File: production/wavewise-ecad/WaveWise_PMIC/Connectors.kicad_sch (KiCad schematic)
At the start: 18 parts, among them J1 24V output, J11 Servo output, J12 Regulated 48V Input, J14 Battery Direct Input, J2 Inverter Inputs, J3 5031590300, J4 5031590400, J5 5031590400, J6 5031590400, J7 5V output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

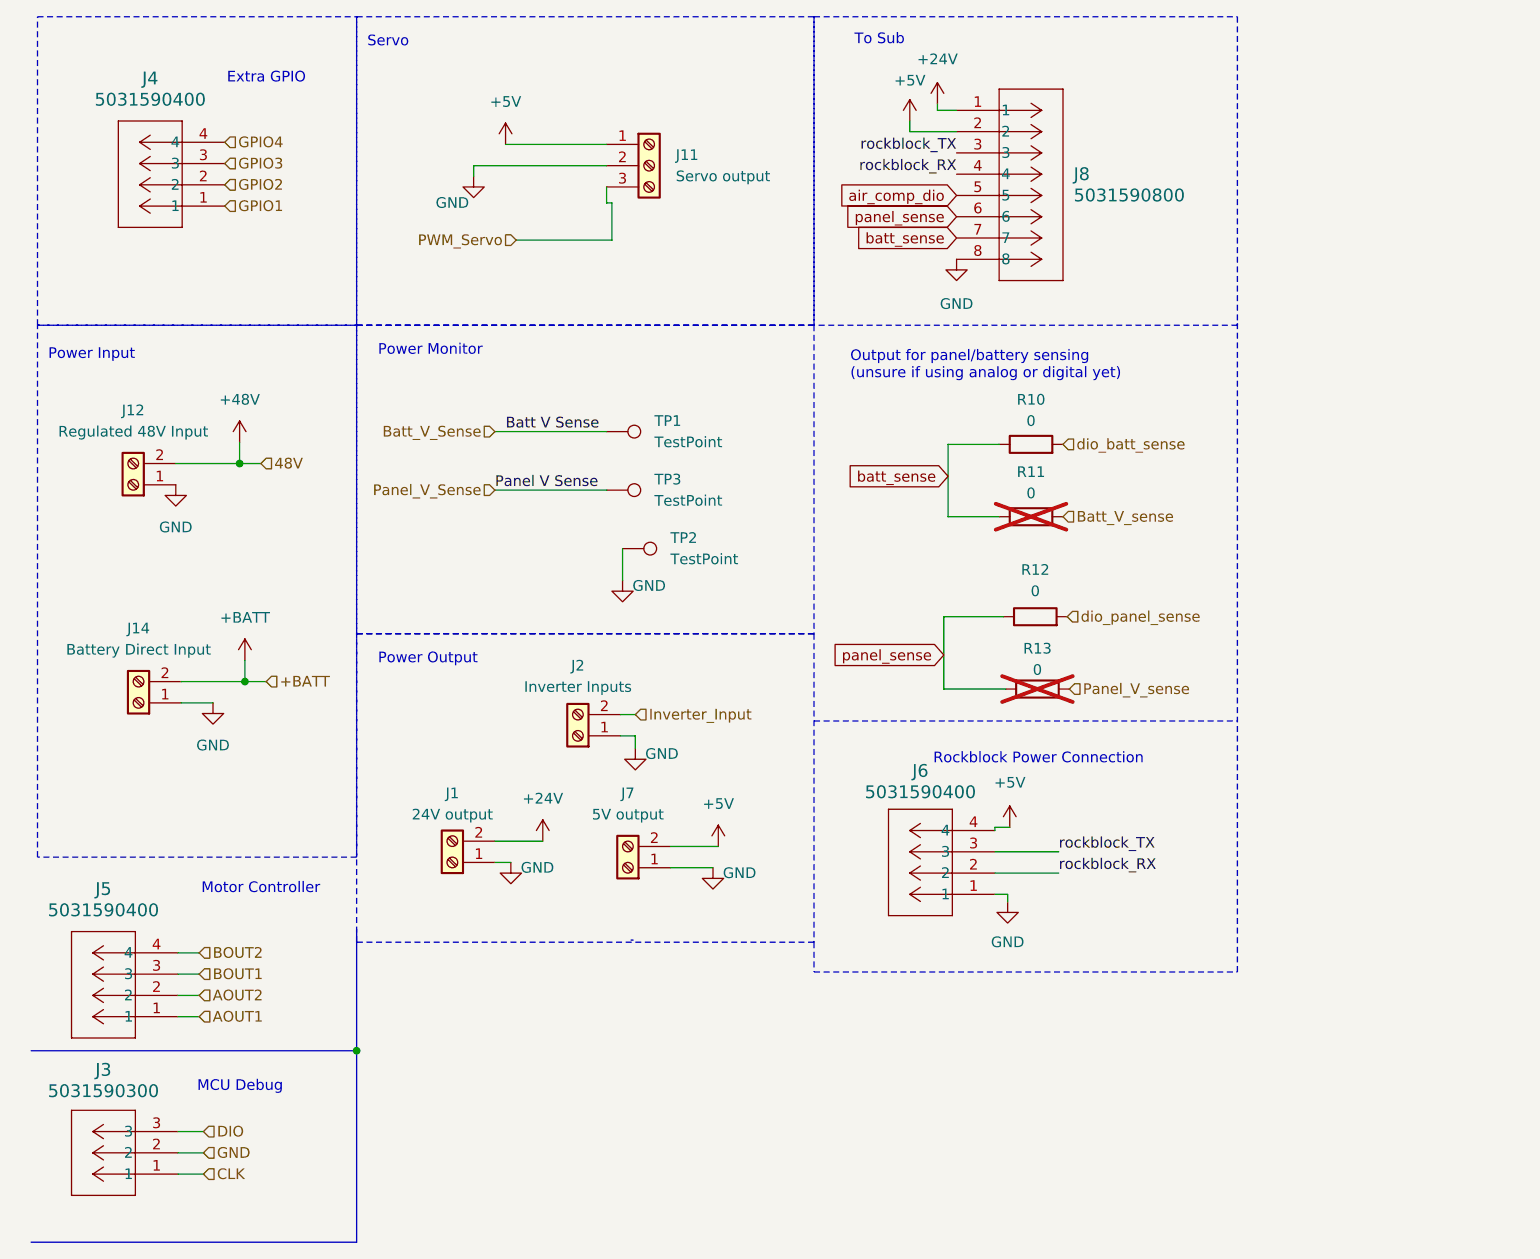
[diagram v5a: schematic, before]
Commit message: Rearranged the whole board
All done aside from no place resistor and  power planes
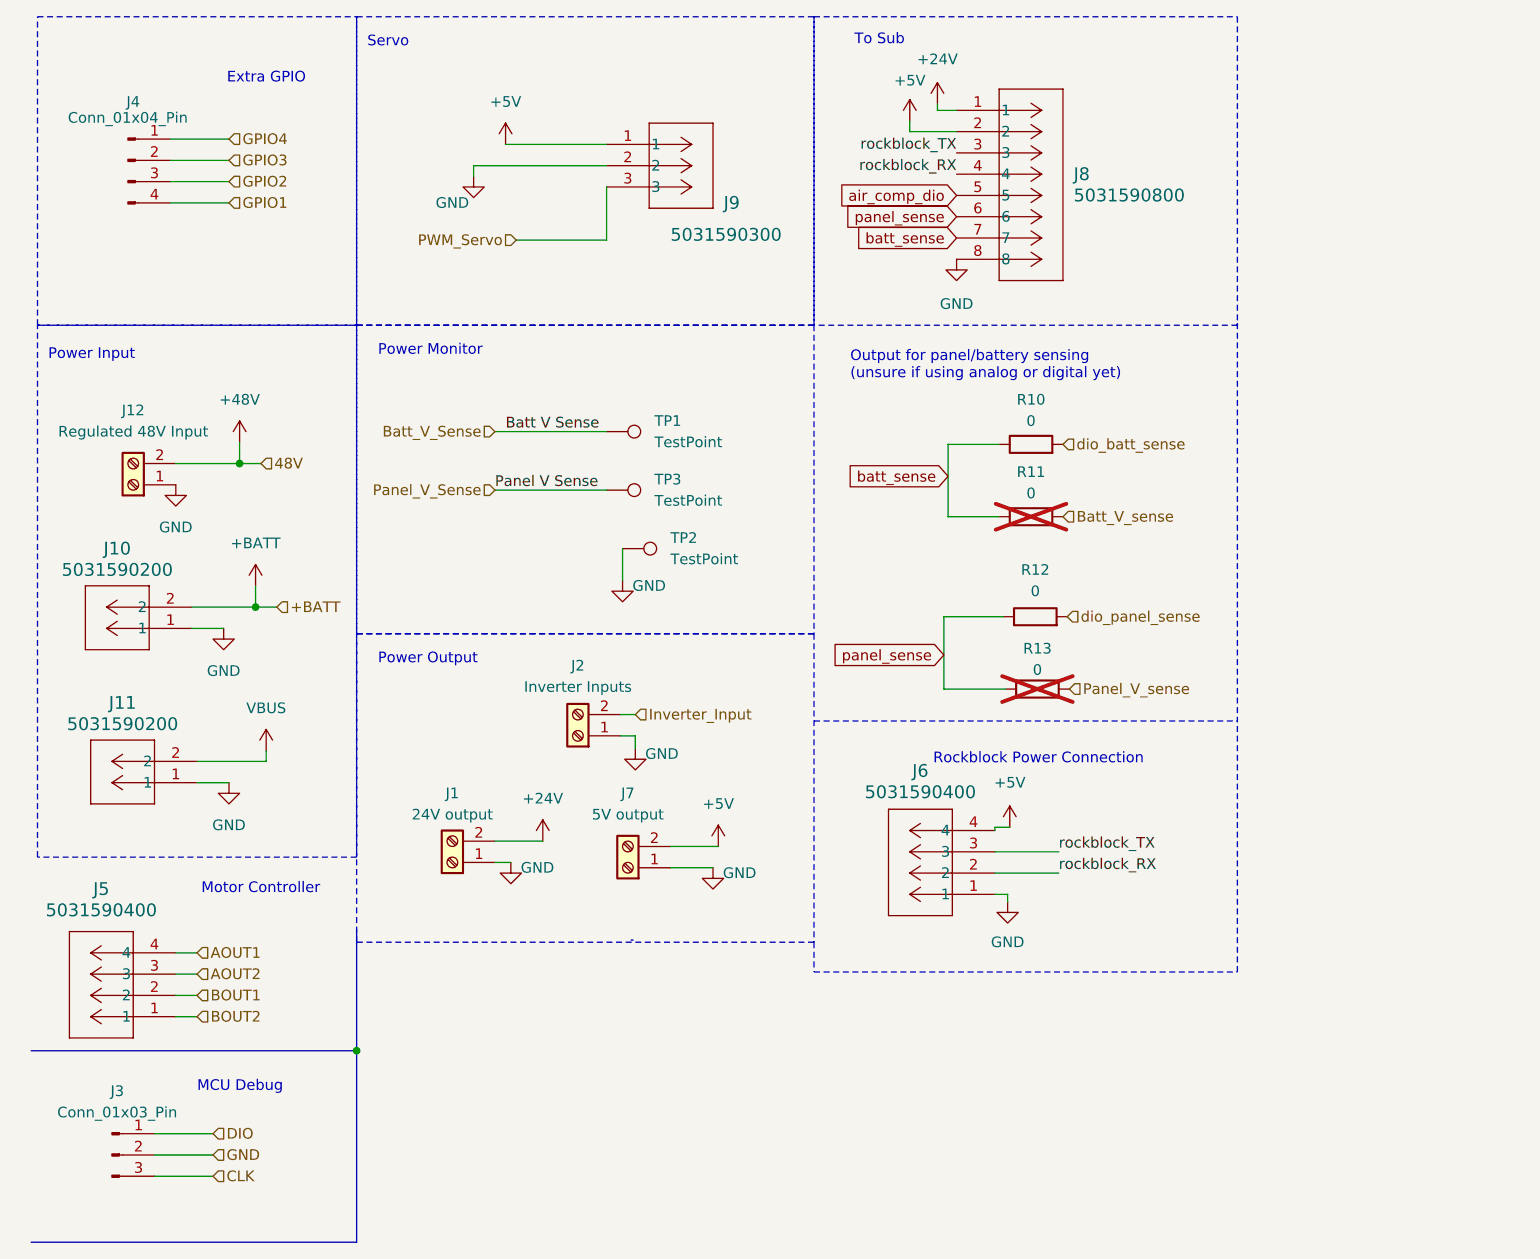
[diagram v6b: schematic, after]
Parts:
- removed J11: Servo output, symbol Connector:Screw_Terminal_01x03
- removed J14: Battery Direct Input, Unchecked:1731721, symbol Connector:Screw_Terminal_01x02
- removed J3: 5031590300, Unchecked:3pinmolex, symbol 3pinmolex:5031590300
- removed J4: 5031590400, Footprints:4pinmolex, symbol 4pinmolex:5031590400
- added J10, J11: 5031590200, Unchecked:2pinmolex, symbol 2pinmolex:5031590200
- added J3: Conn_01x03_Pin, Unchecked:61300311121, symbol Connector:Conn_01x03_Pin
- added J4: Conn_01x04_Pin, Unchecked:61300411121, symbol Connector:Conn_01x04_Pin
- added J9: 5031590300, Unchecked:3pinmolex, symbol 3pinmolex:5031590300
- TP1, TP3: footprint TestPoint:TestPoint_Pad_1.0x1.0mm -> TestPoint:TestPoint_THTPad_1.5x1.5mm_Drill0.7mm
- TP2: footprint TestPoint:TestPoint_Pad_1.5x1.5mm -> TestPoint:TestPoint_THTPad_D2.0mm_Drill1.0mm
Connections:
- net +5V: now also J9.1
- net +BATT: now also J10.2
- net AOUT1: now also J5.4; no longer J5.1
- net AOUT2: now also J5.3; no longer J5.2
- net BOUT1: now also J5.2; no longer J5.3
- net BOUT2: now also J5.1; no longer J5.4
- net CLK: now also J3.3 (Pin_3)
- net DIO: now also J3.1 (Pin_1)
- net GND: now also J10.1, J11.1, J3.2 (Pin_2), J9.2
- net GPIO1: now also J4.4 (Pin_4)
- net GPIO2: now also J4.3 (Pin_3)
- net GPIO3: now also J4.2 (Pin_2)
- net GPIO4: now also J4.1 (Pin_1)
- net PWM_Servo: now also J9.3
- new net VBUS: J11.2

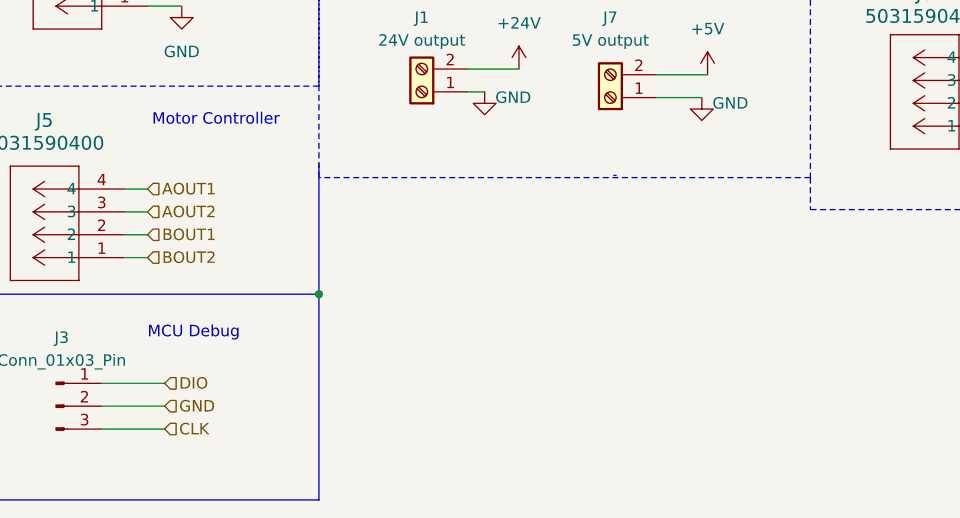
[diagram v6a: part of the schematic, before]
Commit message: Completed all connections and added mounting holes
Needs some review with the DRC tool
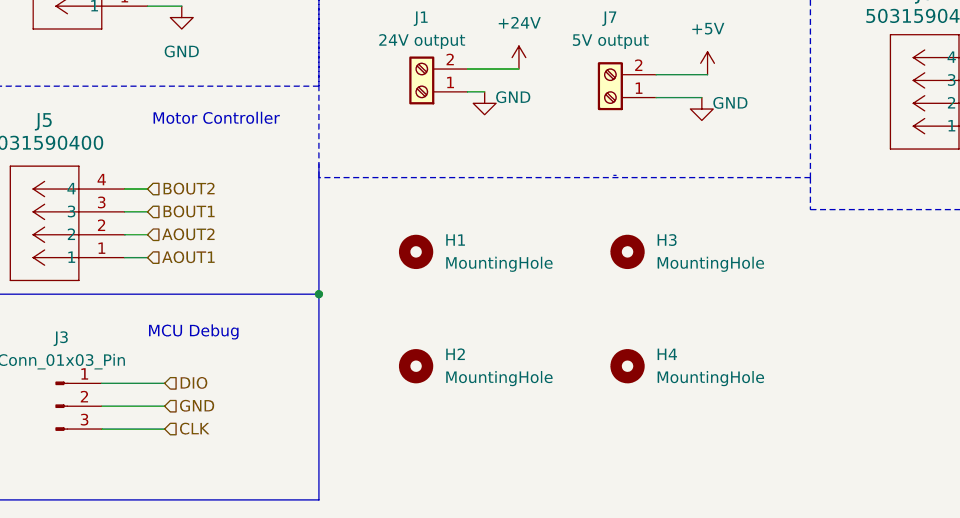
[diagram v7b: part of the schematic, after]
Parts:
- added H1, H2, H3, H4: MountingHole, MountingHole:MountingHole_3.5mm_Pad_TopBottom, symbol Mechanical:MountingHole
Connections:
- net AOUT1: now also J5.1; no longer J5.4
- net AOUT2: now also J5.2; no longer J5.3
- net BOUT1: now also J5.3; no longer J5.2
- net BOUT2: now also J5.4; no longer J5.1
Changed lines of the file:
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@@
-    (stroke (width 0) (type default))
-  )
-  (wire (pts (xy 29.21 127) (xy 31.75 127))
     (stroke (width 0) (type default))
   )
@@
   )
   (wire (pts (xy 80.645 33.02) (xy 80.645 39.37))
-    (stroke (width 0) (type default))
-  )
-  (wire (pts (xy 29.21 129.54) (xy 31.75 129.54))
     (stroke (width 0) (type default))
   )
@@
     (stroke (width 0.15) (type dash))
   )
-  (wire (pts (xy 29.21 124.46) (xy 31.75 124.46))
-    (stroke (width 0) (type default))
-  )
   (polyline (pts (xy 105.41 96.774) (xy 155.956 96.774))
     (stroke (width 0) (type dash))
@@
     (stroke (width 0) (type default))
   )
+  (wire (pts (xy 29.21 129.54) (xy 31.75 129.54))
+    (stroke (width 0) (type default))
+  )
   (wire (pts (xy 35.56 32.385) (xy 28.575 32.385))
     (stroke (width 0) (type default))
@@
     (stroke (width 0) (type default))
   )
+  (wire (pts (xy 29.21 127) (xy 31.75 127))
+    (stroke (width 0) (type default))
+  )
+  (wire (pts (xy 134.62 114.935) (xy 127 114.935))
+    (stroke (width 0) (type default))
+  )
+  (wire (pts (xy 31.75 104.14) (xy 35.56 104.14))
+    (stroke (width 0) (type default))
+  )
   (wire (pts (xy 29.21 132.08) (xy 31.75 132.08))
     (stroke (width 0) (type default))
   )
-  (wire (pts (xy 134.62 114.935) (xy 127 114.935))
-    (stroke (width 0) (type default))
-  )
-  (wire (pts (xy 31.75 104.14) (xy 35.56 104.14))
-    (stroke (width 0) (type default))
-  )
   (wire (pts (xy 29.21 66.04) (xy 36.83 66.04))
     (stroke (width 0) (type default))
@@
   )
   (wire (pts (xy 128.524 117.475) (xy 128.524 118.364))
+    (stroke (width 0) (type default))
+  )
+  (wire (pts (xy 29.21 124.46) (xy 31.75 124.46))
     (stroke (width 0) (type default))
   )
@@
     (effects (font (size 1.27 1.27)) (justify right))
   )
-  (hierarchical_label "BOUT2" (shape input) (at 31.75 132.08 0) (fields_autoplaced)
-    (effects (font (size 1.27 1.27)) (justify left))
-  )
-  (hierarchical_label "AOUT1" (shape input) (at 31.75 124.46 0) (fields_autoplaced)
+  (hierarchical_label "BOUT2" (shape input) (at 31.75 124.46 0) (fields_autoplaced)
+    (effects (font (size 1.27 1.27)) (justify left))
+  )
+  (hierarchical_label "AOUT1" (shape input) (at 31.75 132.08 0) (fields_autoplaced)
     (effects (font (size 1.27 1.27)) (justify left))
   )
@@
     (effects (font (size 1.27 1.27)) (justify left))
   )
-  (hierarchical_label "AOUT2" (shape input) (at 31.75 127 0) (fields_autoplaced)
+  (hierarchical_label "AOUT2" (shape input) (at 31.75 129.54 0) (fields_autoplaced)
     (effects (font (size 1.27 1.27)) (justify left))
   )
@@
     (effects (font (size 1.27 1.27)) (justify left))
   )
-  (hierarchical_label "BOUT1" (shape input) (at 31.75 129.54 0) (fields_autoplaced)
+  (hierarchical_label "BOUT1" (shape input) (at 31.75 127 0) (fields_autoplaced)
     (effects (font (size 1.27 1.27)) (justify left))
   )
@@
     )
   )
+  (symbol (lib_id "Mechanical:MountingHole") (at 85.09 144.145 0) (unit 1)
+    (in_bom yes) (on_board yes) (dnp no) (fields_autoplaced)
+    (property "Reference" "H4" (at 88.265 142.875 0)
+      (effects (font (size 1.27 1.27)) (justify left))
+    )
+    (property "Value" "MountingHole" (at 88.265 145.415 0)
+      (effects (font (size 1.27 1.27)) (justify left))
+    )
+    (property "Footprint" "MountingHole:MountingHole_3.5mm_Pad_TopBottom" (at 85.09 144.145 0)
+      (effects (font (size 1.27 1.27)) hide)
+    )
+    (property "Datasheet" "~" (at 85.09 144.145 0)
+      (effects (font (size 1.27 1.27)) hide)
+    )
+    (instances
+      (project "WaveWise_PMIC"
+        (path "/8343c01b-8940-4cb8-a17d-91fd7fb1cccd/7fd42481-dc5a-4ae0-adec-c5e7a3228be9"
+          (reference "H4") (unit 1)
+        )
+      )
+    )
+  )
   (symbol (lib_id "Connector:TestPoint") (at 82.55 76.2 270) (unit 1)
     (in_bom yes) (on_board yes) (dnp no) (fields_autoplaced)
@@
     )
   )
+  (symbol (lib_id "Mechanical:MountingHole") (at 61.595 131.445 0) (unit 1)
+    (in_bom yes) (on_board yes) (dnp no) (fields_autoplaced)
+    (property "Reference" "H1" (at 64.77 130.175 0)
+      (effects (font (size 1.27 1.27)) (justify left))
+    )
+    (property "Value" "MountingHole" (at 64.77 132.715 0)
+      (effects (font (size 1.27 1.27)) (justify left))
+    )
+    (property "Footprint" "MountingHole:MountingHole_3.5mm_Pad_TopBottom" (at 61.595 131.445 0)
+      (effects (font (size 1.27 1.27)) hide)
+    )
+    (property "Datasheet" "~" (at 61.595 131.445 0)
+      (effects (font (size 1.27 1.27)) hide)
+    )
+    (instances
+      (project "WaveWise_PMIC"
+        (path "/8343c01b-8940-4cb8-a17d-91fd7fb1cccd/7fd42481-dc5a-4ae0-adec-c5e7a3228be9"
+          (reference "H1") (unit 1)
+        )
+      )
+    )
+  )
   (symbol (lib_id "power:+48V") (at 36.83 63.5 0) (unit 1)
     (in_bom yes) (on_board yes) (dnp no) (fields_autoplaced)
@@
         (path "/8343c01b-8940-4cb8-a17d-91fd7fb1cccd/7fd42481-dc5a-4ae0-adec-c5e7a3228be9"
           (reference "#PWR027") (unit 1)
+        )
+      )
+    )
+  )
+  (symbol (lib_id "Mechanical:MountingHole") (at 85.09 131.445 0) (unit 1)
+    (in_bom yes) (on_board yes) (dnp no) (fields_autoplaced)
+    (property "Reference" "H3" (at 88.265 130.175 0)
+      (effects (font (size 1.27 1.27)) (justify left))
+    )
+    (property "Value" "MountingHole" (at 88.265 132.715 0)
+      (effects (font (size 1.27 1.27)) (justify left))
+    )
+    (property "Footprint" "MountingHole:MountingHole_3.5mm_Pad_TopBottom" (at 85.09 131.445 0)
+      (effects (font (size 1.27 1.27)) hide)
+    )
+    (property "Datasheet" "~" (at 85.09 131.445 0)
+      (effects (font (size 1.27 1.27)) hide)
+    )
+    (instances
+      (project "WaveWise_PMIC"
+        (path "/8343c01b-8940-4cb8-a17d-91fd7fb1cccd/7fd42481-dc5a-4ae0-adec-c5e7a3228be9"
+          (reference "H3") (unit 1)
         )
       )
@@
         )
       )
+    )
+  )
+  (symbol (lib_id "Mechanical:MountingHole") (at 61.595 144.145 0) (unit 1)
+    (in_bom yes) (on_board yes) (dnp no) (fields_autoplaced)
+    (property "Reference" "H2" (at 64.77 142.875 0)
+      (effects (font (size 1.27 1.27)) (justify left))
+    )
+    (property "Value" "MountingHole" (at 64.77 145.415 0)
+      (effects (font (size 1.27 1.27)) (justify left))
+    )
+    (property "Footprint" "MountingHole:MountingHole_3.5mm_Pad_TopBottom" (at 61.595 144.145 0)
+      (effects (font (size 1.27 1.27)) hide)
+    )
+    (property "Datasheet" "~" (at 61.595 144.145 0)
+      (effects (font (size 1.27 1.27)) hide)
+    )
+    (instances
+      (project "WaveWise_PMIC"
+        (path "/8343c01b-8940-4cb8-a17d-91fd7fb1cccd/7fd42481-dc5a-4ae0-adec-c5e7a3228be9"
+          (reference "H2") (unit 1)
+        )
+      )

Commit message: Prelim board layout
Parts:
- removed H3: MountingHole, MountingHole:MountingHole_3.5mm_Pad_TopBottom, symbol Mechanical:MountingHole
- removed J12: Regulated 48V Input, Unchecked:1731721, symbol Connector:Screw_Terminal_01x02
- removed J2: Inverter Inputs, Unchecked:1731721, symbol Connector:Screw_Terminal_01x02
- removed J4: Conn_01x04_Pin, Unchecked:61300411121, symbol Connector:Conn_01x04_Pin
- removed J7: 5V output, Unchecked:2pinmolex, symbol Connector:Screw_Terminal_01x02
- added 3V1: TestPoint, TestPoint:TestPoint_Pad_D1.5mm, symbol Connector:TestPoint
- added HE1: MountingHole, MountingHole:MountingHole_3.2mm_M3_ISO7380_Pad, symbol Mechanical:MountingHole
- added J13: Screw_Terminal_01x03, Unchecked:CONN_1731734_PXC, symbol Connector:Screw_Terminal_01x03
- added J2: Conn_01x06_Pin, Unchecked:61300611121, symbol Connector:Conn_01x06_Pin
- added R15, R16, R18, R19, R20, R21, R22, R23, R25, R26: 0, Resistor_SMD:R_0805_2012Metric, symbol Device:R
- H1, H2, H4: footprint MountingHole:MountingHole_3.5mm_Pad_TopBottom -> MountingHole:MountingHole_3.2mm_M3_ISO7380_Pad
- J5, J6: footprint Footprints:4pinmolex -> Unchecked:4pinmolex
- J8: footprint Footprints:8pinmolex -> Unchecked:8pinmolex
- renumbered TP1 to BatteryV1, TP2 to GND1, TP3 to PanelV1
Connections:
- net Batt_V_sense is gone; now on net Batt_V_Sense: R11.2
- net Panel_V_sense is gone; now on net Panel_V_Sense: R13.2
- net +48V: now also J13.3 (Pin_3)
- net +5V: now also J2.5 (Pin_5)
- net GND: now also J13.1 (Pin_1), J2.6 (Pin_6), R20.1, R21.1, R22.1, R23.1
- net GPIO1: now also J2.4 (Pin_4)
- net GPIO2: now also J2.3 (Pin_3)
- net GPIO3: now also J2.2 (Pin_2)
- net GPIO4: now also J2.1 (Pin_1)
- net Inverter_Input: now also R26.2
- net air_comp_dio: now also R25.1
- net rockblock_RX: now also J6.3, R15.1, R16.2; no longer J6.2, J8.4
- net rockblock_TX: now also J6.2, R18.1, R19.1; no longer J6.3, J8.3
- net CLK renamed SWDIO
- net DIO renamed SWCLK
- net dio_batt_sense renamed BATT_SENSE_DIO
- net dio_panel_sense renamed PANEL_SENSE_DIO
- new net: H2.1, R21.2
- new net: H1.1, R20.2
- new net: J13.2 (Pin_2), R25.2, R26.1
- new net: HE1.1, R22.2
- new net: H4.1, R23.2
- new net +3.3V: 3V1.1
- new net BICO_UART_RX: R16.1
- new net BICO_UART_TX: R19.2
- new net SICO_RX: J8.4, R15.2
- new net SICO_TX: J8.3, R18.2
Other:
- moved on the sheet: BatteryV1, J6, J8, R11
